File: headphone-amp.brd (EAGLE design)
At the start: 32 x 53.3 mm, 46 parts, among them IC1 OPA1612, J1 USB4125-GF-A_REVA, J3 PJ-3200, J4 PJ-3200, J5 PJ-3200, U1 TPS65131

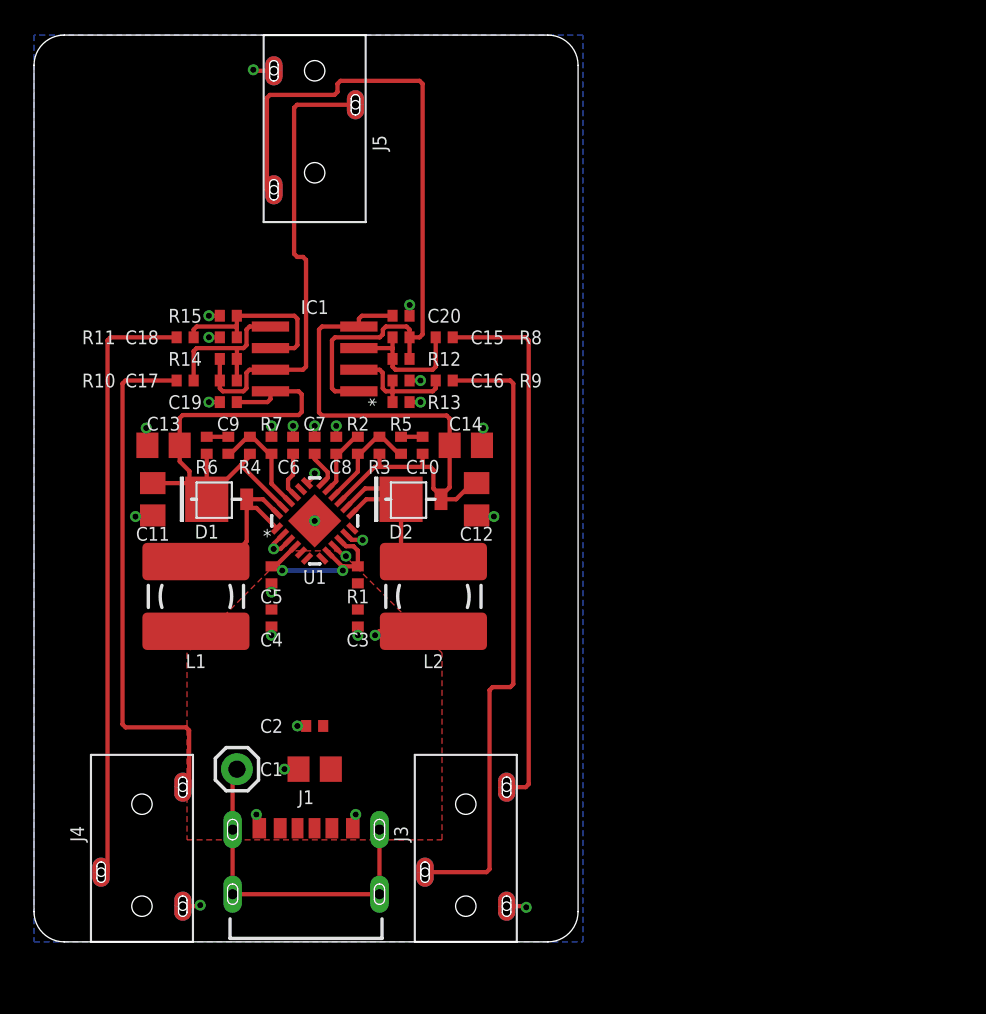
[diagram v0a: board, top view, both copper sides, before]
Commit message: add power led, add soft start, fix op amp polarity
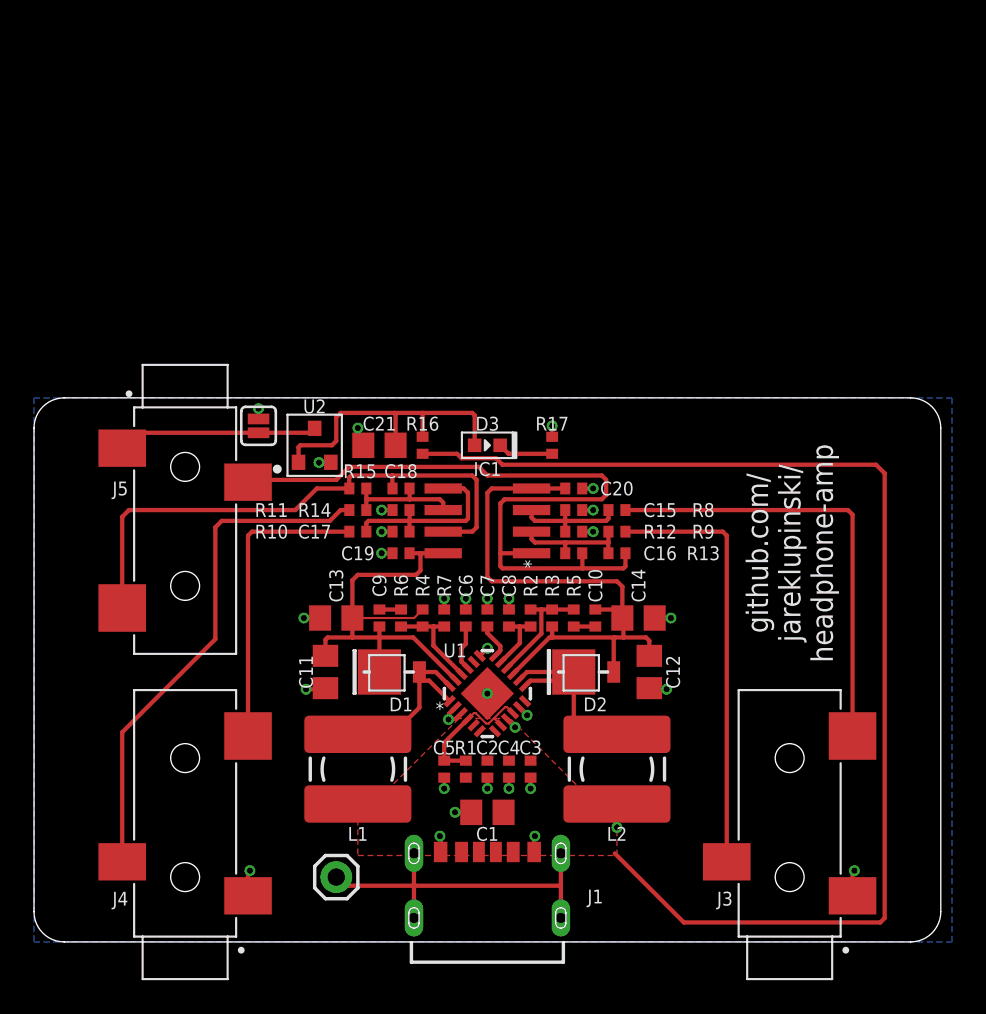
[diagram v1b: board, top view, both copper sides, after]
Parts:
- added C21: 22uF / 25V, rcl:C0805
- added D3: Red, MF_LEDs:LED0603
- added JP1: JUMPER-SMT_2_NO_SILK, SparkFun-Jumpers:SMT-JUMPER_2_NO_SILK
- added R16: 100k, rcl:R0402
- added R17: 10k, rcl:R0402
- added U2: 2N7002, MF_Discrete_Semiconductor:SOT-23-3
- J3, J4, J5: value PJ-3200 -> SJ-3523-SMT-TR; device sonik:PJ-3200 -> SJ-3523-SMT-TR:CUI_SJ-3523-SMT-TR
- R2: value 88k -> 81k
- moved J5 26.5 mm to (8.89, 27.9)
- moved J3 19.4 mm to (44.5, 3.81)
- moved C4 16.6 mm to (27.9, 10.2)
- moved R13 15.5 mm to (34.3, 22.9)
- moved C5 15.3 mm to (24.1, 10.2)
- moved R6 15.3 mm to (21.6, 19.1)
- moved L2 14.8 mm to (34.3, 10.2)
- moved C10 14.4 mm to (33.0, 19.1), turned to 270 degrees
- moved C14 14.4 mm to (35.6, 19.1)
- moved C15 14.4 mm to (31.8, 25.4)
- moved C16 14.4 mm to (31.8, 22.9)
- moved R11 14.4 mm to (19.1, 25.4)
- moved R8 14.4 mm to (34.3, 25.4)
- moved C11 14.4 mm to (17.1, 15.9)
- moved C12 14.4 mm to (36.2, 15.9)
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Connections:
- removed net N$2: C1.2, C2.2, C3.1, C4.2, J1.A9, J1.B9, L1.1, R1.1, U1.P5, U1.P6
- removed net N$23 (its old number): C15.1, IC1.1, J5.4, R12.1
- new net N$1: C18.1, IC1.7, J5.2, R15.1
- new net N$25: J5.1, JP1.2, U2.P$3
- new net N$26: C21.1, D3.ANODE, R16.1, U2.P$1
- new net N$4: C16.1, IC1.1, J5.3, R13.1
- new net VIN: C1.2, C2.2, C3.1, C4.2, J1.A9, J1.B9, L1.1, R1.1, R16.2, U1.P5, U1.P6
- net GND: now also C15.1, C17.1, C21.2, J3.1, J4.1, JP1.1, R12.1, R14.1, R17.1, U2.P$2; no longer C16.1, C18.1, J3.3, J4.3, J5.3, R13.1, R15.1
- net N$12: now also R8.2; no longer R9.2
- net N$18: now also J4.2; no longer J4.4
- net N$19: now also J4.3; no longer J4.2
- net N$20: now also D3.CATHODE, R17.2; no longer C17.1, IC1.7, J5.2, R14.1
- net N$6: now also J3.3, R9.2; no longer J3.4, R8.2
- net N$7: now also R6.2; no longer C9.1
- net VDD: now also C9.1; no longer R6.2
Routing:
- net VIN: track 0.00 -> 71.5 mm
- net N$4: track 0.00 -> 43.7 mm
- net N$23 (its old number): track 42.3 -> 0.00 mm
- net N$1: track 0.00 -> 33.3 mm
- net N$20: track 27.0 -> 3.26 mm
- net N$26: track 0.00 -> 18.1 mm
- net N$18: track 30.7 -> 17.8 mm
- net N$25: track 0.00 -> 11.8 mm
- net N$12: track 36.9 -> 26.5 mm
- net N$6: track 31.6 -> 25.2 mm
- net N$19: track 35.4 -> 30.2 mm
- net N$16: track 11.2 -> 6.95 mm
- net VDD: track 30.3 -> 27.3 mm
- net N$23: track 10.9 -> 8.49 mm, vias 2 -> 0
- net N$17: track 9.30 -> 11.0 mm
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- added copper zone on layer 1, net VIN
- removed copper zone on layer 1, net N$2
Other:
- board size 32 x 53.3 mm -> 53.3 x 32 mm
- board text added: "github.com/ jareklupinski/ headphone-amp"

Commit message: little routing change
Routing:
- net VDD: track 27.3 -> 28.0 mm
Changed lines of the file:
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@@
 <contactref element="C10" pad="1"/>
 <wire x1="28.179671875" y1="15.76111875" x2="30.325553125" y2="17.907" width="0.254" layer="1"/>
-<wire x1="34.671" y1="17.907" x2="34.671" y2="18.989" width="0.254" layer="1"/>
 <wire x1="34.671" y1="18.989" x2="34.61" y2="19.05" width="0.254" layer="1"/>
 <wire x1="30.325553125" y1="17.907" x2="30.48" y2="17.907" width="0.254" layer="1"/>
-<wire x1="30.48" y1="17.907" x2="34.163" y2="17.907" width="0.254" layer="1"/>
-<wire x1="34.163" y1="17.907" x2="34.671" y2="17.907" width="0.254" layer="1"/>
-<wire x1="34.101" y1="15.875" x2="34.101" y2="17.845" width="0.254" layer="1"/>
-<wire x1="34.101" y1="17.845" x2="34.163" y2="17.907" width="0.254" layer="1"/>
-<wire x1="36.195" y1="16.825" x2="36.195" y2="17.714" width="0.254" layer="1"/>
-<wire x1="36.195" y1="17.714" x2="36.002" y2="17.907" width="0.254" layer="1"/>
-<wire x1="36.002" y1="17.907" x2="34.671" y2="17.907" width="0.254" layer="1"/>
 <wire x1="30.48" y1="18.55" x2="30.48" y2="17.907" width="0.254" layer="1"/>
 <wire x1="33.02" y1="19.55" x2="34.11" y2="19.55" width="0.254" layer="1"/>
@@
 <wire x1="26.924" y1="21.209" x2="34.295" y2="21.209" width="0.254" layer="1"/>
 <wire x1="34.295" y1="21.209" x2="34.61" y2="20.894" width="0.254" layer="1"/>
+<wire x1="30.48" y1="17.907" x2="34.163" y2="17.907" width="0.254" layer="1"/>
+<wire x1="34.163" y1="17.907" x2="34.544" y2="17.907" width="0.254" layer="1"/>
+<wire x1="34.544" y1="17.907" x2="34.671" y2="18.034" width="0.254" layer="1"/>
+<wire x1="34.671" y1="18.034" x2="34.671" y2="18.989" width="0.254" layer="1"/>
+<wire x1="34.101" y1="15.875" x2="34.101" y2="16.383" width="0.254" layer="1"/>
+<wire x1="34.101" y1="16.383" x2="34.101" y2="17.845" width="0.254" layer="1"/>
+<wire x1="34.101" y1="17.845" x2="34.163" y2="17.907" width="0.254" layer="1"/>
+<wire x1="36.195" y1="16.825" x2="35.753" y2="16.383" width="0.254" layer="1"/>
+<wire x1="35.753" y1="16.383" x2="34.101" y2="16.383" width="0.254" layer="1"/>
 </signal>
 <signal name="VDD">
@@
 <wire x1="24.806771875" y1="15.407565625" x2="22.3073375" y2="17.907" width="0.254" layer="1"/>
 <wire x1="22.3073375" y1="17.907" x2="20.32" y2="17.907" width="0.254" layer="1"/>
-<wire x1="20.32" y1="17.907" x2="18.73" y2="17.907" width="0.254" layer="1"/>
-<wire x1="18.73" y1="17.907" x2="18.73" y2="19.05" width="0.254" layer="1"/>
-<wire x1="17.145" y1="16.825" x2="17.145" y2="17.78" width="0.254" layer="1"/>
 <wire x1="20.32" y1="18.55" x2="20.32" y2="17.907" width="0.254" layer="1"/>
-<wire x1="20.32" y1="15.875" x2="20.32" y2="17.907" width="0.254" layer="1"/>
-<wire x1="17.145" y1="17.78" x2="17.272" y2="17.907" width="0.254" layer="1"/>
-<wire x1="17.272" y1="17.907" x2="18.73" y2="17.907" width="0.254" layer="1"/>
+<wire x1="20.32" y1="15.875" x2="20.32" y2="16.51" width="0.254" layer="1"/>
+<wire x1="20.32" y1="16.51" x2="20.32" y2="17.907" width="0.254" layer="1"/>
 <wire x1="22.09" y1="22.86" x2="22.733" y2="22.86" width="0.254" layer="1"/>
 <wire x1="22.733" y1="22.86" x2="24.07" y2="22.86" width="0.254" layer="1"/>
@@
 <wire x1="22.733" y1="21.844" x2="22.733" y2="22.86" width="0.254" layer="1"/>
 <wire x1="22.479" y1="21.59" x2="22.733" y2="21.844" width="0.254" layer="1"/>
+<wire x1="17.145" y1="16.825" x2="20.005" y2="16.825" width="0.254" layer="1"/>
+<wire x1="20.005" y1="16.825" x2="20.32" y2="16.51" width="0.254" layer="1"/>
+<wire x1="18.73" y1="19.05" x2="18.73" y2="17.973" width="0.254" layer="1"/>
+<wire x1="18.73" y1="17.973" x2="18.796" y2="17.907" width="0.254" layer="1"/>
+<wire x1="18.796" y1="17.907" x2="20.32" y2="17.907" width="0.254" layer="1"/>
 </signal>
 <signal name="N$21">
